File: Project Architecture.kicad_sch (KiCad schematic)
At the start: 0 parts

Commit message: SCH[Cleaning]:Updated Connectors not sure still, added sprate bat and ground connections, updated commincation conncetors. PCB[Layout]:Inital layout of compents need to fit on board size once tap connecton method is decided.
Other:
- sheet Connectors ports: added VMODULE; removed none
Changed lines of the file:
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@@
 	(title_block
 		(title "Project Architecture")
-		(date "2025-01-12")
 		(rev "${REVISION}")
 		(company "${COMPANY}")
@@
 		)
 	)
+	(junction
+		(at 106.68 60.96)
+		(diameter 0)
+		(color 0 0 0 0)
+	)
 	(wire
 		(pts
@@
 		)
 	)
+	(wire
+		(pts
+			(xy 185.42 58.42) (xy 185.42 60.96)
+		)
+		(stroke
+			(width 0)
+			(type default)
+		)
+	)
 	(bus
 		(pts
@@
 	(wire
 		(pts
+			(xy 185.42 60.96) (xy 190.5 60.96)
+		)
+		(stroke
+			(width 0)
+			(type default)
+		)
+	)
+	(wire
+		(pts
 			(xy 190.5 129.54) (xy 187.96 129.54)
 		)
@@
 	(wire
 		(pts
+			(xy 106.68 60.96) (xy 114.3 60.96)
+		)
+		(stroke
+			(width 0)
+			(type default)
+		)
+	)
+	(wire
+		(pts
 			(xy 187.96 129.54) (xy 187.96 132.08)
 		)
@@
 	(bus
 		(pts
-			(xy 177.8 60.96) (xy 190.5 60.96)
+			(xy 177.8 68.58) (xy 190.5 68.58)
 		)
 		(stroke
@@
 	(wire
 		(pts
-			(xy 101.6 60.96) (xy 114.3 60.96)
+			(xy 101.6 60.96) (xy 106.68 60.96)
 		)
 		(stroke
@@
 		(pts
 			(xy 152.4 78.74) (xy 149.86 78.74)
+		)
+		(stroke
+			(width 0)
+			(type default)
+		)
+	)
+	(wire
+		(pts
+			(xy 106.68 58.42) (xy 106.68 60.96)
 		)
 		(stroke
@@
 	)
 	(symbol
+		(lib_id "power:VSSA")
+		(at 106.68 58.42 0)
+		(unit 1)
+		(body_style 1)
+		(exclude_from_sim no)
+		(in_bom yes)
+		(on_board yes)
+		(in_pos_files yes)
+		(dnp no)
+		(property "Reference" "#PWR054"
+			(at 106.68 62.23 0)
+			(hide yes)
+			(show_name no)
+			(do_not_autoplace no)
+			(effects
+				(font
+					(size 1.27 1.27)
+				)
+			)
+		)
+		(property "Value" "VMODULE"
+			(at 106.68 54.61 0)
+			(show_name no)
+			(do_not_autoplace no)
+			(effects
+				(font
+					(size 1.27 1.27)
+				)
+			)
+		)
+		(property "Footprint" ""
+			(at 106.68 58.42 0)
+			(hide yes)
+			(show_name no)
+			(do_not_autoplace no)
+			(effects
+				(font
+					(size 1.27 1.27)
+				)
+			)
+		)
+		(property "Datasheet" ""
+			(at 106.68 58.42 0)
+			(hide yes)
+			(show_name no)
+			(do_not_autoplace no)
+			(effects
+				(font
+					(size 1.27 1.27)
+				)
+			)
+		)
+		(property "Description" "Power symbol creates a local label with name \"VSSA\""
+			(at 106.68 58.42 0)
+			(hide yes)
+			(show_name no)
+			(do_not_autoplace no)
+			(effects
+				(font
+					(size 1.27 1.27)
+				)
+			)
+		)
+		(pin "1"
+		)
+		(instances
+			(project "bms_slave"
+				(path "/f9e05184-c88b-4a88-ae9c-ab2bdb32be7c/c5103ceb-5325-4a84-a025-9638a412984e"
+					(reference "#PWR054")
+					(unit 1)
+				)
+			)
+		)
+	)
+	(symbol
 		(lib_id "power:GND")
 		(at 149.86 81.28 0)
@@
 		)
 	)
+	(symbol
+		(lib_id "power:VSSA")
+		(at 185.42 58.42 0)
+		(unit 1)
+		(body_style 1)
+		(exclude_from_sim no)
+		(in_bom yes)
+		(on_board yes)
+		(in_pos_files yes)
+		(dnp no)
+		(property "Reference" "#PWR055"
+			(at 185.42 62.23 0)
+			(hide yes)
+			(show_name no)
+			(do_not_autoplace no)
+			(effects
+				(font
+					(size 1.27 1.27)
+				)
+			)
+		)
+		(property "Value" "VMODULE"
+			(at 185.42 54.61 0)
+			(show_name no)
+			(do_not_autoplace no)
+			(effects
+				(font
+					(size 1.27 1.27)
+				)
+			)
+		)
+		(property "Footprint" ""
+			(at 185.42 58.42 0)
+			(hide yes)
+			(show_name no)
+			(do_not_autoplace no)
+			(effects
+				(font
+					(size 1.27 1.27)
+				)
+			)
+		)
+		(property "Datasheet" ""
+			(at 185.42 58.42 0)
+			(hide yes)
+			(show_name no)
+			(do_not_autoplace no)
+			(effects
+				(font
+					(size 1.27 1.27)
+				)
+			)
+		)
+		(property "Description" "Power symbol creates a local label with name \"VSSA\""
+			(at 185.42 58.42 0)
+			(hide yes)
+			(show_name no)
+			(do_not_autoplace no)
+			(effects
+				(font
+					(size 1.27 1.27)
+				)
+			)
+		)
+		(pin "1"
+		)
+		(instances
+			(project "bms_slave"
+				(path "/f9e05184-c88b-4a88-ae9c-ab2bdb32be7c/c5103ceb-5325-4a84-a025-9638a412984e"
+					(reference "#PWR055")
+					(unit 1)
+				)
+			)
+		)
+	)
 	(sheet
 		(at 152.4 55.88)
@@
 		)
 		(pin "T_P[1..8]" passive
-			(at 177.8 60.96 0)
+			(at 177.8 68.58 0)
 			(effects
 				(font
@@
 		)
 		(pin "T_P[1..8]" passive
-			(at 190.5 60.96 180)
+			(at 190.5 68.58 180)
 			(effects
 				(font
@@
 					(size 1.27 1.27)
 					(color 0 0 0 1)
+				)
+				(justify left)
+			)
+		)
+		(pin "VMODULE" passive
+			(at 190.5 60.96 180)
+			(effects
+				(font
+					(size 1.27 1.27)
 				)
 				(justify left)
@@
 	)
 	(sheet
-		(at 233.68 54.61)
+		(at 228.6 57.15)
 		(size 25.4 25.4)
 		(exclude_from_sim no)
@@
 		)
 		(fill
-			(color 0 0 0 0)
+			(color 255 255 194 1)
 		)
 		(property "Sheetname" "Mechanical"
-			(at 233.68 53.34 0)
+			(at 228.6 55.88 0)
 			(show_name no)
 			(do_not_autoplace no)
@@
 		)
 		(property "Sheetfile" "mechanical.kicad_sch"
-			(at 233.68 80.5946 0)
-			(hide yes)
-			(show_name no)
+			(at 228.6 83.1346 0)
+			(hide yes)
+			(show_name no)

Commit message: PCB[Mounting]: Messing with mounting holes for board to board connection. SCH[Naming]: Small naming changes, T_P -> TMP
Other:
- sheet Connectors ports: added TMP[1..8]; removed T_P[1..8]
- sheet Temperature Sense ports: added TMP[1..8]; removed T_P[1..8]
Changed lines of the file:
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@@
 			)
 		)
-		(pin "T_P[1..8]" passive
+		(pin "TMP[1..8]" passive
 			(at 177.8 68.58 0)
 			(effects
@@
 			)
 		)
-		(pin "T_P[1..8]" passive
+		(pin "TMP[1..8]" passive
 			(at 190.5 68.58 180)
 			(effects

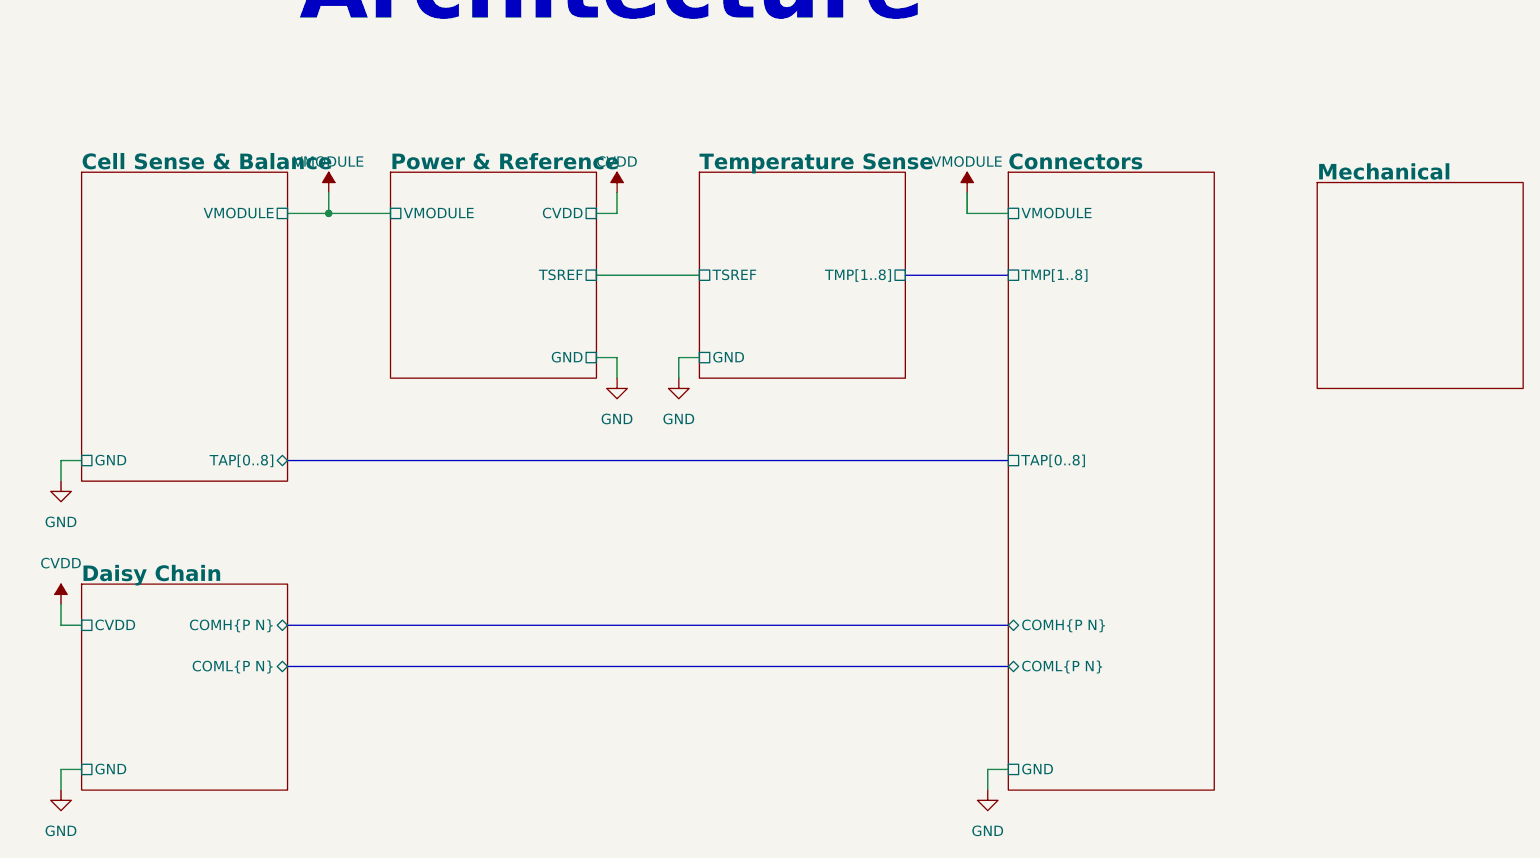
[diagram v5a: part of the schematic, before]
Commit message: PCB[Grounding, Heat]: Added some more pours for heat considerations for bjt, stiched more vias for heat consideration on balanace resistors. SCH[Notes, Block Diagram]: Working on spelling and notes updates, started block diagram.
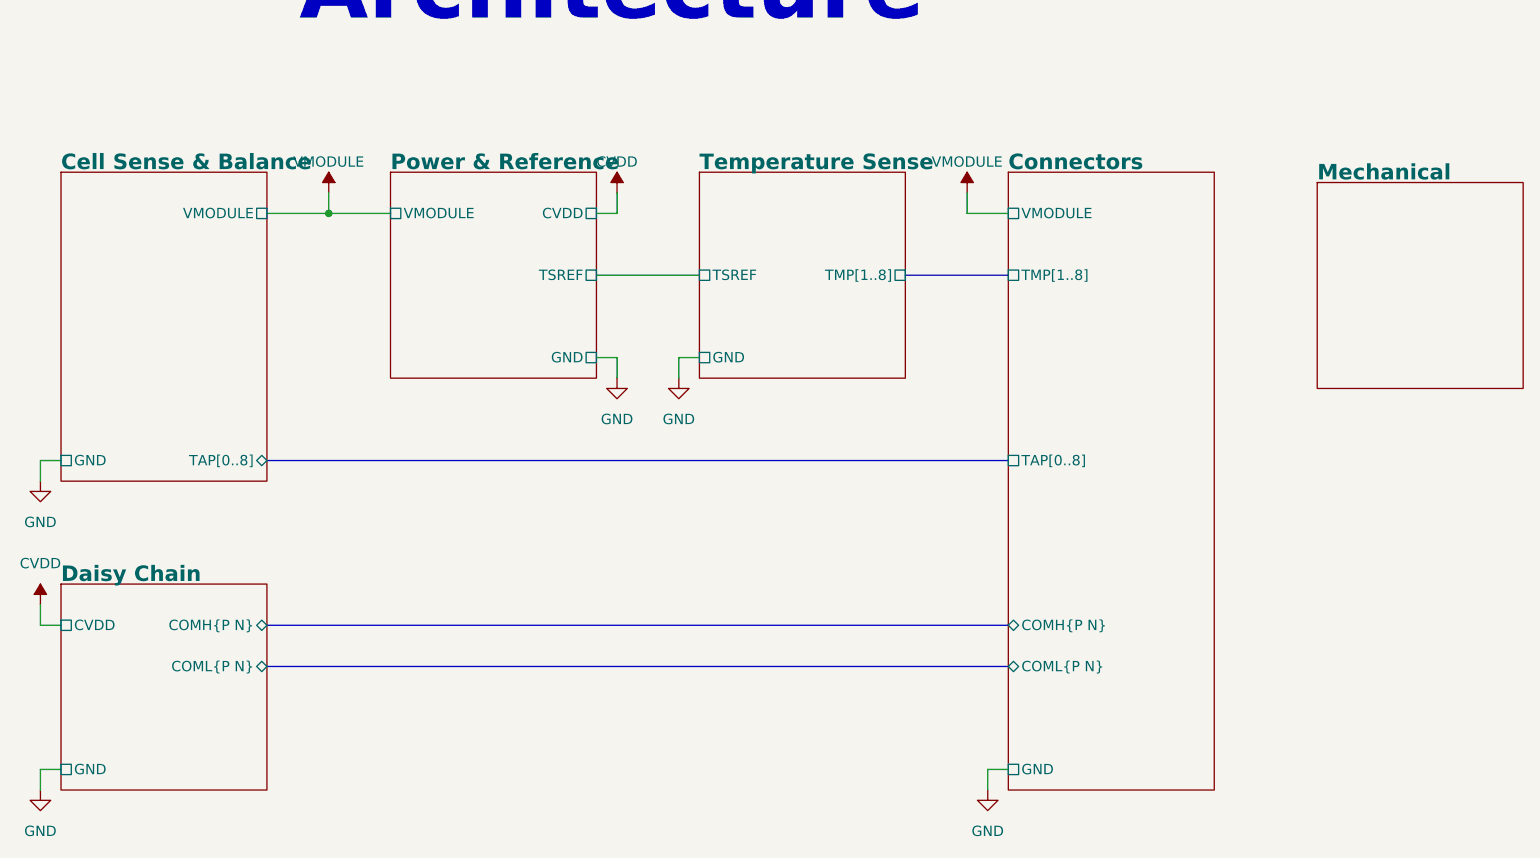
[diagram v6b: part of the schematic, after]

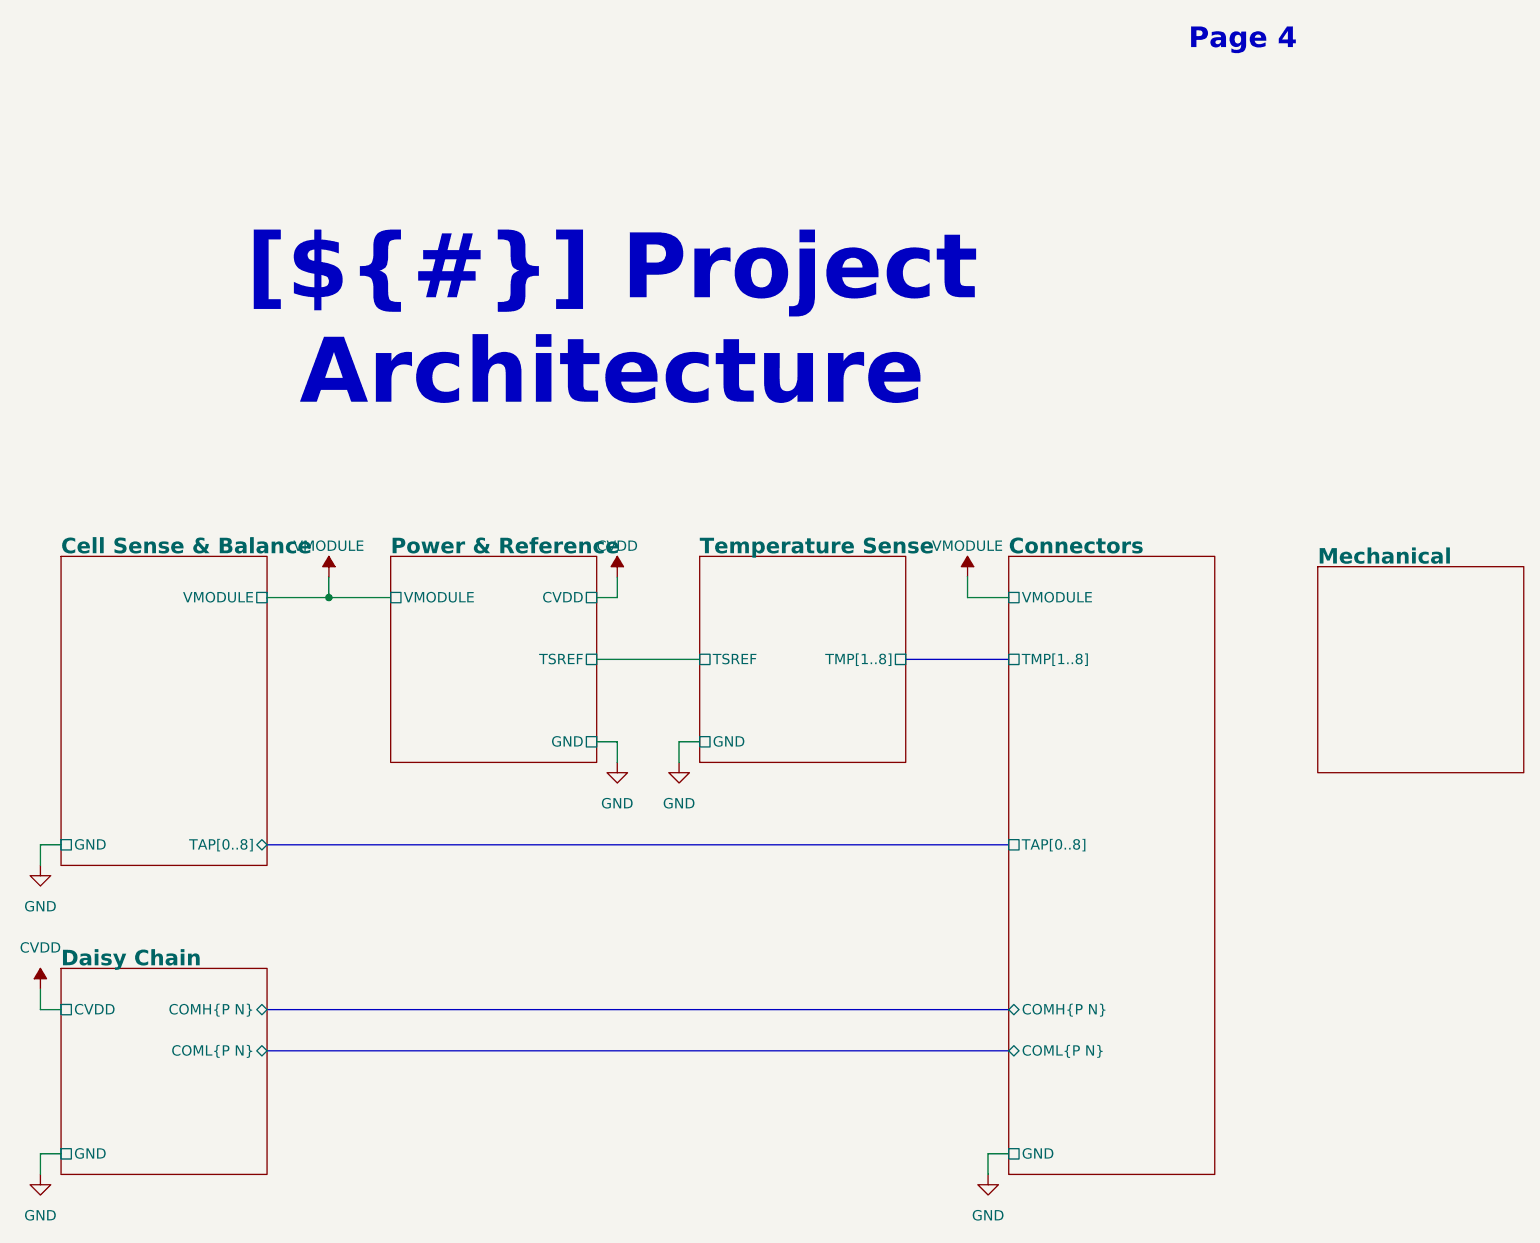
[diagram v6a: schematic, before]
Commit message: PCB[Test Points, Mechanical, Silk]: Finalized Mounting Points, Added Testpoints with adjecent silkscreen labels. SCH[Test Points, Notes]: Added/Updated notes for all pages, cleaned up errors spelling ect.
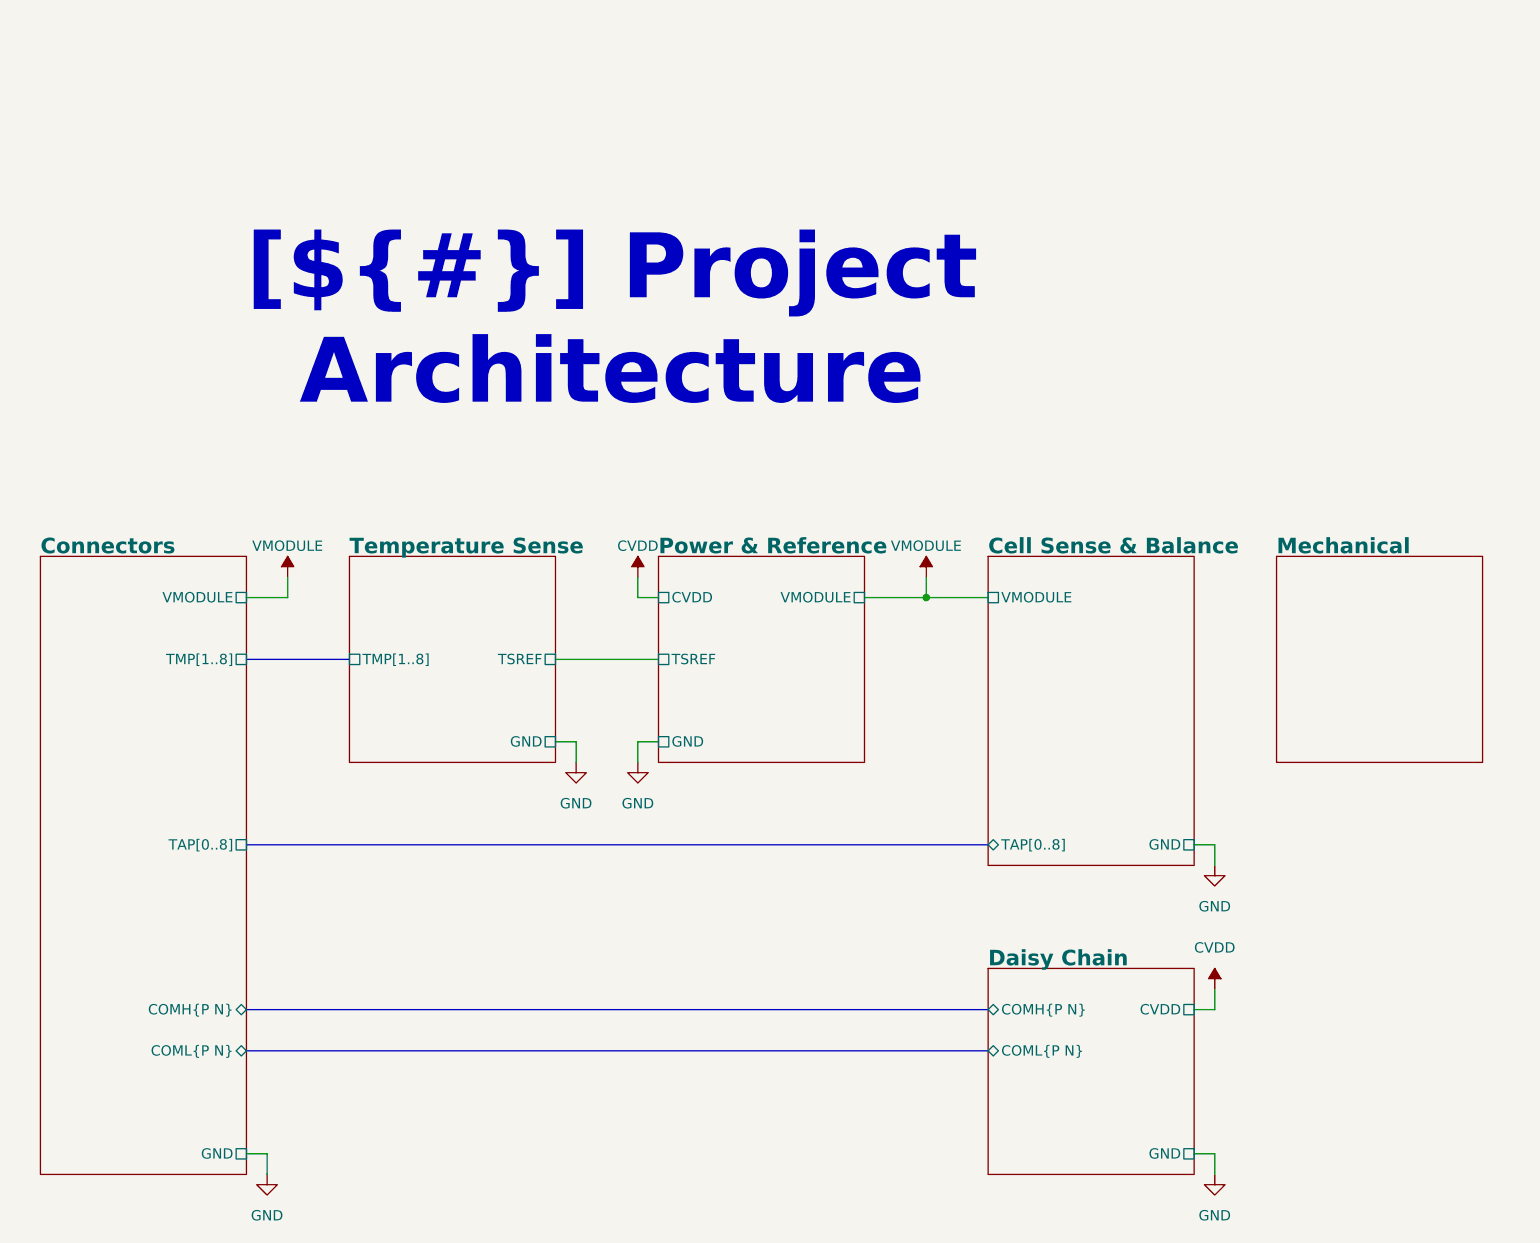
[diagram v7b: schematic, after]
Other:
- note removed: "Page 4"
